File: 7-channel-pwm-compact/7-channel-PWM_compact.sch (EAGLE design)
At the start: 18 parts, among them J1 POWER_JACKSLT

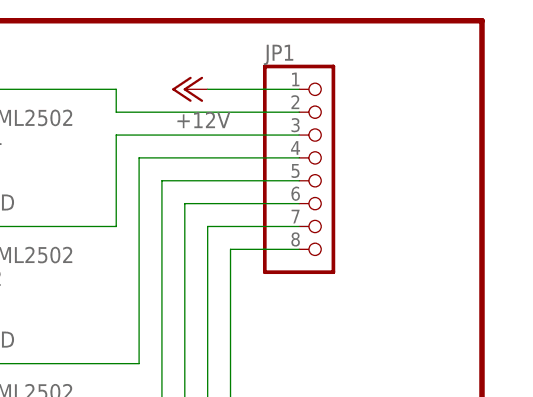
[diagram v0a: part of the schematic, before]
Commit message: update 7 channel pwm design
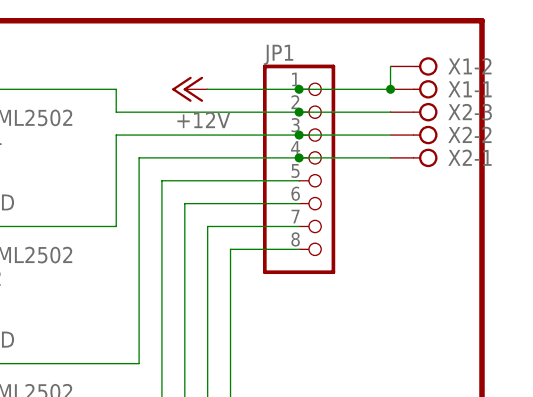
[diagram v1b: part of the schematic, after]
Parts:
- added X1: (no value), con-wago-508:W237-02P
- added X2: (no value), con-wago-508:W237-03P
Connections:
- net +12V: now also X1-1.KL, X1-2.KL
- net N$2: now also X2-3.KL
- net N$4: now also X2-2.KL
- net N$5: now also X2-1.KL
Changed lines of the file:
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@@
 <part name="GND9" library="supply1" deviceset="GND" device=""/>
 <part name="GND10" library="supply1" deviceset="GND" device=""/>
+<part name="X1" library="con-wago-508" deviceset="W237-02P" device=""/>
+<part name="X2" library="con-wago-508" deviceset="W237-03P" device=""/>
 </parts>
 <sheets>
@@
 <attribute name="VALUE" x="212.344" y="-5.842" size="1.778" layer="96"/>
 </instance>
+<instance part="X1" gate="-1" x="226.06" y="53.34" rot="R180"/>
+<instance part="X1" gate="-2" x="226.06" y="55.88" rot="R180"/>
+<instance part="X2" gate="-1" x="226.06" y="45.72" rot="R180"/>
+<instance part="X2" gate="-2" x="226.06" y="48.26" rot="R180"/>
+<instance part="X2" gate="-3" x="226.06" y="50.8" rot="R180"/>
 </instances>
 <busses>
@@
 <pinref part="U$4" gate="G$1" pin="D"/>
 <wire x1="190.5" y1="53.34" x2="170.18" y2="53.34" width="0.1524" layer="91"/>
+<wire x1="210.82" y1="50.8" x2="220.98" y2="50.8" width="0.1524" layer="91"/>
+<junction x="210.82" y="50.8"/>
+<pinref part="X2" gate="-3" pin="KL"/>
 </segment>
 </net>
@@
 <pinref part="U$2" gate="G$1" pin="D"/>
 <wire x1="190.5" y1="38.1" x2="170.18" y2="38.1" width="0.1524" layer="91"/>
+<wire x1="220.98" y1="48.26" x2="210.82" y2="48.26" width="0.1524" layer="91"/>
+<junction x="210.82" y="48.26"/>
+<pinref part="X2" gate="-2" pin="KL"/>
 </segment>
 </net>
@@
 <pinref part="U$3" gate="G$1" pin="D"/>
 <wire x1="193.04" y1="22.86" x2="170.18" y2="22.86" width="0.1524" layer="91"/>
+<wire x1="210.82" y1="45.72" x2="220.98" y2="45.72" width="0.1524" layer="91"/>
+<junction x="210.82" y="45.72"/>
+<pinref part="X2" gate="-1" pin="KL"/>
 </segment>
 </net>
@@
 <pinref part="JP1" gate="A" pin="1"/>
 <wire x1="200.66" y1="53.34" x2="210.82" y2="53.34" width="0.1524" layer="91"/>
-</segment>
-<segment>
+<pinref part="X1" gate="-1" pin="KL"/>
+<wire x1="210.82" y1="53.34" x2="220.98" y2="53.34" width="0.1524" layer="91"/>
+<junction x="210.82" y="53.34"/>
+<pinref part="X1" gate="-2" pin="KL"/>
+<wire x1="220.98" y1="53.34" x2="220.98" y2="55.88" width="0.1524" layer="91"/>
+<junction x="220.98" y="53.34"/>
+</segment>
+<segment>
